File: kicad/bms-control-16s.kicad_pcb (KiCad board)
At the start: 2 copper layers, 120 x 65 mm, 131 parts, among them J1 TempBtn, J2 UEXT, J3 USB_B_Micro, J4 CAN, J5 Conn_02x09_Top_Bottom, J6 Conn_02x06_Odd_Even, J7 Conn_01x17, J8 Conn_01x02, P5 CONN_01X02, Q1 FCX495TA, U1 AP2210-3.3, U2 LMR16030, U3 STM32G0B1CETxN, U4 BQ76952, U5 ESP32-C3-MINI-1, U6 TJA1042T-3, Y1 8MHz

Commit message: v0.1 design ready for review
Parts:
- removed C34: 100n, LibreSolar:C_0603_1608
- removed D10: USBLC6-2SC6, LibreSolar:SOT-23-6
- removed J6: Conn_02x06_Odd_Even, Connector_PinSocket_2.54mm:PinSocket_2x06_P2.54mm_Vertical
- removed J7: Conn_01x17, Connector_PinHeader_2.54mm:PinHeader_1x17_P2.54mm_Vertical
- removed JP1: Jumper_NC_Small, Connector_PinHeader_2.54mm:PinHeader_1x02_P2.54mm_Vertical
- removed P5: CONN_01X02, Connector_PinHeader_2.54mm:PinHeader_1x02_P2.54mm_Vertical
- removed the REF** at (84.0, 101.0)
- removed SWD1: ST_Nucleo_SWD_5p, Connector_PinHeader_2.54mm:PinHeader_1x05_P2.54mm_Vertical
- added C44: 1µF, LibreSolar:C_0603_1608, F.Cu at (147.6, 61.4)
- added C45: 100pF, LibreSolar:C_0603_1608, F.Cu at (174.0, 67.5)
- added D9: D_Schottky, Diode_SMD:D_SOD-128, F.Cu at (133.0, 106.0)
- added FID1: Fiducial, Fiducial:Fiducial_1mm_Mask2mm, F.Cu at (101.0, 117.5)
- added FID2: Fiducial, Fiducial:Fiducial_1mm_Mask2mm, F.Cu at (179.9, 65.2)
- added J10: Conn_01x06, Connector_PinSocket_2.00mm:PinSocket_1x06_P2.00mm_Vertical, B.Cu at (156.0, 64.0)
- added J9: Conn_01x06, Connector_PinSocket_2.00mm:PinSocket_1x06_P2.00mm_Vertical, B.Cu at (156.0, 111.0)
- added TP10: CHG, TestPoint:TestPoint_Pad_D1.5mm, F.Cu at (159.0, 114.2)
- added TP11: CAN_H, TestPoint:TestPoint_Pad_D1.5mm, F.Cu at (120.5, 73.4)
- added TP12: SHUT, TestPoint:TestPoint_Pad_D1.5mm, F.Cu at (150.4, 58.8)
- added TP13: ALERT, TestPoint:TestPoint_Pad_D1.5mm, F.Cu at (150.4, 63.6)
- added TP14: SW_PWR, TestPoint:TestPoint_Pad_D1.5mm, F.Cu at (119.1, 104.9)
- added TP15: WAKE, TestPoint:TestPoint_Pad_D1.5mm, F.Cu at (130.8, 90.7)
- added TP2: CAN_L, TestPoint:TestPoint_Pad_D1.5mm, F.Cu at (117.9, 72.1)
- added TP3: REG1, TestPoint:TestPoint_Pad_D1.5mm, F.Cu at (156.5, 60.5)
- added TP4: PDSG, TestPoint:TestPoint_Pad_D1.5mm, F.Cu at (159.5, 60.5)
- added TP8: DSG, TestPoint:TestPoint_Pad_D1.5mm, F.Cu at (162.5, 60.5)
- added TP9: CD, TestPoint:TestPoint_Pad_D1.5mm, F.Cu at (162.2, 114.2)
- C27: value 100p -> 100pF
- C28: value 100n -> 100nF
- C30: value 470nF -> 680nF
- D1: value BAV70 -> 100V; footprint LibreSolar:SOT-23 -> Diode_SMD:D_SOD-123
- D6: value BAV70 -> D_Schottky; footprint LibreSolar:SOT-23 -> Diode_SMD:D_SOD-123F
- H1, H2, H3: footprint MountingHole:MountingHole_3.2mm_M3_Pad -> MountingHole:MountingHole_3.2mm_M3
- J1: value TempBtn -> MicroFit 2x7; footprint Connector_Molex:Molex_Micro-Fit_3.0_43045-0600_2x03_P3.00mm_Horizontal -> Connector_Molex:Molex_Micro-Fit_3.0_43045-1410_2x07-1MP_P3.00mm_Horizontal
- J4: value CAN -> Conn_01x06; footprint Connector_Molex:Molex_Micro-Fit_3.0_43045-0600_2x03_P3.00mm_Horizontal -> LibreSolar:Wuerth_WR-WST_2x03_P2.54_DBG
- J5: value Conn_02x09_Top_Bottom -> MicroFit 2x9; footprint Connector_Molex:Molex_Micro-Fit_3.0_43045-1800_2x09_P3.00mm_Horizontal -> Connector_Molex:Molex_Micro-Fit_3.0_43045-1810_2x09-1MP_P3.00mm_Horizontal
- R18, R21: footprint LibreSolar:R_0603_1608 -> LibreSolar:R_1206_3216
- R25: value 120 -> 1M; footprint LibreSolar:R_1206_3216 -> LibreSolar:R_0603_1608
- TP1: footprint TestPoint:TestPoint_Pad_D2.0mm -> TestPoint:TestPoint_Pad_D1.5mm
- TP5: value Regout -> REG1; footprint LibreSolar:TestPoint_1mm_pad -> TestPoint:TestPoint_Pad_D1.5mm
- TP6, TP7: footprint LibreSolar:TestPoint_1mm_pad -> TestPoint:TestPoint_Pad_D1.5mm
- moved H3 98.2 mm to (178.0, 116.0)
- moved LOGO1 92.1 mm to (170.6, 59.5)
- moved S1 64.0 mm to (104.5, 109.0), turned to 180 degrees
- moved R54 59.5 mm to (111.5, 104.0), turned to 180 degrees
- moved H2 58.7 mm to (178.0, 59.0)
- moved R53 57.3 mm to (111.5, 102.5), turned to 0 degrees
- moved LOGO2 54.7 mm to (143.2, 97.9)
- moved H1 53.3 mm to (119.0, 87.5)
- moved TP7 51.1 mm to (105.9, 75.3)
- moved TP6 50.5 mm to (108.6, 75.3)
- moved R25 48.9 mm to (139.5, 112.0), turned to 180 degrees
- moved J4 48.5 mm to (135.4, 66.2), turned to -90 degrees
- moved R26 43.7 mm to (144.1, 56.1), turned to 180 degrees
- moved C46 42.3 mm to (100.5, 62.5), turned to 90 degrees
- moved REF** 41.0 mm to (172.5, 108.0)
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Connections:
- net Net-(C39-Pad1) renamed /BQ76952/BREG_IN
- C37 pad 1: /BQ76952/REG1 -> /REG1
- D1 pad 1: /BAT+ -> /Power Supply/VIN
- D1 pad 2: unconnected-(D1-Pad2) -> /BAT+
- D2 pad 2: /CHG+ -> /CD
- D3 pad 2: Net-(D3-Pad2) -> /USB_D-
- D4 pad 2: Net-(D4-Pad2) -> /USB_D+
- D6 pad 1: /Power Supply/RGO -> +5V
- D6 pad 2: +5V -> /BQ76952/REG2
- D8 pad 3: unconnected-(D8-Pad3) -> GND
- J1 pad 1: /TEMP1 -> GND
- J1 pad 2: /TEMP2 -> GND
- J1 pad 4: GND -> unconnected-(J1-Pad4)
- J1 pad 6: /BTN_2 -> /CAN_L
- J3 pad 2: Net-(D3-Pad2) -> /USB_D-
- J3 pad 3: Net-(D4-Pad2) -> /USB_D+
- J4 pad 1: /CAN_H -> +3V3
- J4 pad 2: /CAN_L -> /SWDIO
- J4 pad 4: /CAN_H -> /SWCLK
- J4 pad 5: /CAN_L -> /DBG_RX
- J4 pad 6: GND -> /DBG_TX
- R20 pad 1: /PGND -> /PACK-
- R22 pad 2: /LED1 -> /LED_RED
- R23 pad 2: /LED2 -> /LED_GREEN
- R25 pad 1: Net-(JP1-Pad2) -> /Power Supply/VIN
- R25 pad 2: /CAN_L -> /REG1
- R32 pad 1: /USB_D- -> /ESP_USB_D-
- R32 pad 2: Net-(D3-Pad2) -> /USB_D-
- R33 pad 1: /USB_D+ -> /ESP_USB_D+
- R33 pad 2: Net-(D4-Pad2) -> /USB_D+
- R35 pad 2: /STM32 MCU/BOOT0 -> /SWCLK
- R55 pad 2: /STM32 MCU/I2C2_PULLUP -> +3V3
- R56 pad 2: /STM32 MCU/I2C2_PULLUP -> +3V3
- TP5 pad 1: /Power Supply/RGO -> /REG1
- U2 pad 3: /Power Supply/EN -> /REG1
- U3 pad 20: unconnected-(U3-Pad20) -> /BQ76952/RST_SHUT
- U3 pad 29: /STM32 MCU/USART1_TX -> /DBG_TX
- U3 pad 32: /STM32 MCU/USART1_RX -> /DBG_RX
- U3 pad 33: /STM32 MCU/USB_DM -> /USB_D-
- U3 pad 34: /STM32 MCU/USB_DP -> /USB_D+
- U3 pad 35: /STM32 MCU/SWDIO -> /SWDIO
- U3 pad 36: /STM32 MCU/SWCLK -> /SWCLK
- U4 pad 34: unconnected-(U4-Pad34) -> /BQ76952/REG2
- U4 pad 35: /BQ76952/REG1 -> /REG1
- U4 pad 40: /BQ76952/PCHG -> unconnected-(U4-Pad40)
- U5 pad 26: /USB_D- -> /ESP_USB_D-
- U5 pad 27: /USB_D+ -> /ESP_USB_D+
- U5 pad 30: /UEXT_RX -> /DBG_RX
- U5 pad 31: /UEXT_TX -> /DBG_TX
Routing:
- net +3V3: track 0.00 -> 189.4 mm, vias 0 -> 11
- net +5V: track 0.00 -> 144.3 mm, vias 0 -> 2
- net /ALERT: track 0.00 -> 108.2 mm, vias 0 -> 7
- net /SW_PWR: track 0.00 -> 101.4 mm, vias 0 -> 5
- net /LED_RED: track 0.00 -> 96.4 mm, vias 0 -> 4
- net /TEMP4: track 0.00 -> 90.8 mm
- net /LED_GREEN: track 0.00 -> 88.8 mm, vias 0 -> 4
- net /BTN_1: track 0.00 -> 82.4 mm, vias 0 -> 3
- net /REG1: track 0.00 -> 75.7 mm
- net GND: track 0.00 -> 72.7 mm, vias 1 -> 82
- net /CHG: track 0.00 -> 62.2 mm
- net /BQ_MISO_SDA: track 0.00 -> 59.4 mm, vias 0 -> 5
- net /BQ_SCK_SCL: track 0.00 -> 57.0 mm, vias 0 -> 5
- net /TEMP2: track 0.00 -> 56.5 mm, vias 0 -> 2
- net /DBG_RX: track 0.00 -> 56.1 mm, vias 0 -> 3
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- added copper zone on F.Cu, net +5V
- added copper zone on F.Cu, net /BQ76952/BREG_IN
- added copper zone on F.Cu, net /Power Supply/VIN
- added copper zone on F.Cu, net GND
- removed copper zone on F.Cu, net +3V3
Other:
- board size 120 x 65 mm -> 88 x 65 mm
- board text added: "2-layer PCB 35µm copper thickness Silkscreen top only"
- board text added: "v0.1"
- board text removed: "2-layer PCB 70µm copper thickness Silkscreen top only"

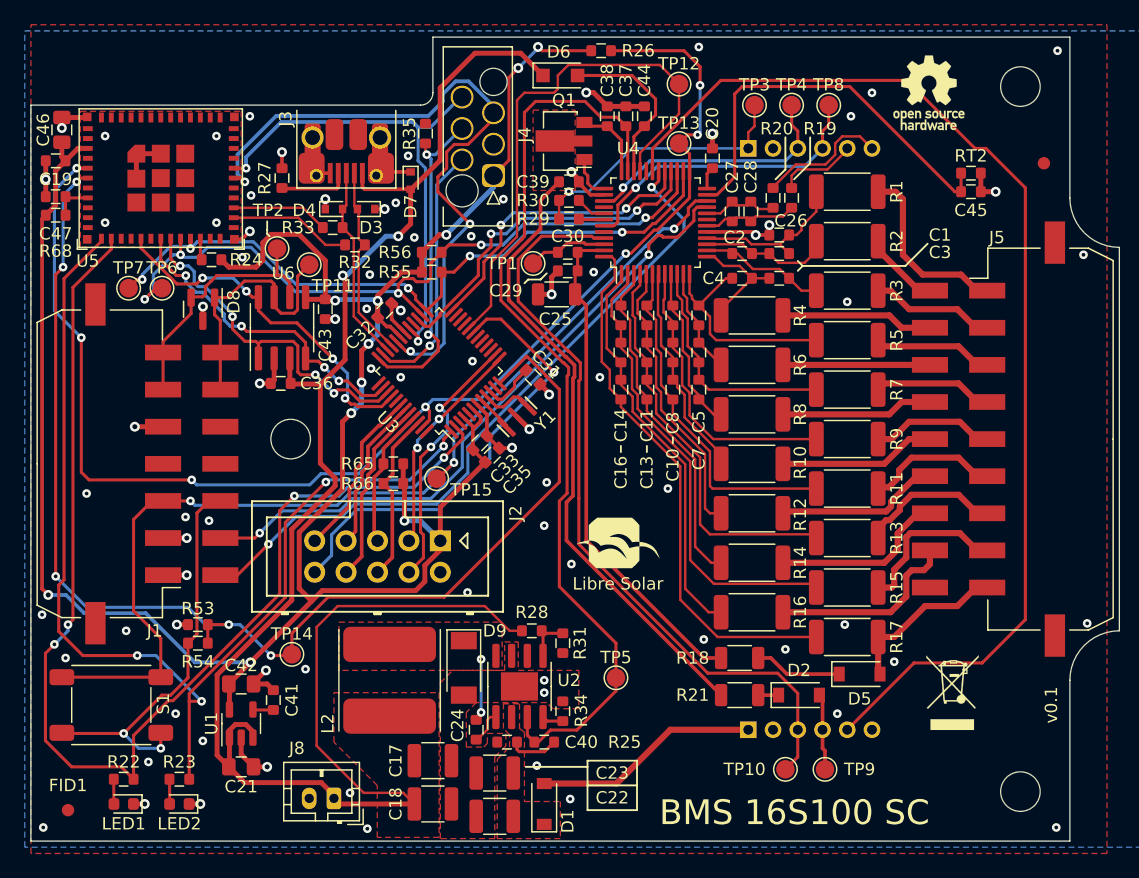
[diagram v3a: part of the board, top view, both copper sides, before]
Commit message: Updates based on review comments (v0.2)
This is the design revision that was ordered for the first prototype build.

The pinout of the cell connector and the board-to-board connector changed
compared to v0.1, hence it got a minor revision update.

The control board is now a 4-layer board to improve the grounding of the
PCB. Various other suggested improvements from the design review are also
included in this update.

Fixes #11, #12, #13, #17, #18, #19
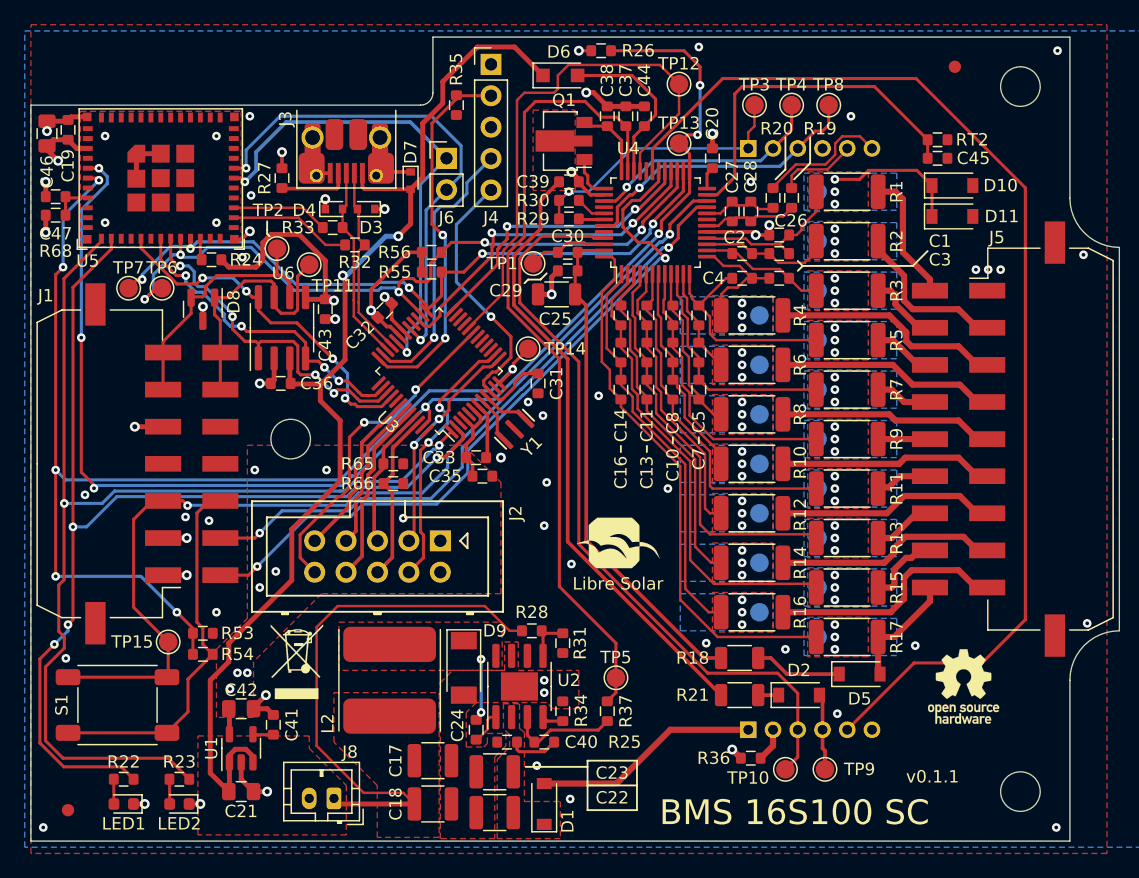
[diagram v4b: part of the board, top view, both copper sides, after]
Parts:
- added D10: 100V, Diode_SMD:D_SOD-123, F.Cu at (172.5, 67.0)
- added D11: 3.6V, Diode_SMD:D_SOD-123, F.Cu at (172.5, 69.5)
- added J6: Conn_01x02, Connector_PinHeader_2.54mm:PinHeader_1x02_P2.54mm_Vertical, F.Cu at (131.6, 64.8)
- added R36: 0R, LibreSolar:R_0603_1608, F.Cu at (156.2, 113.3)
- added R37: 0R, LibreSolar:R_0603_1608, F.Cu at (144.6, 109.5)
- added TP16: TestPoint, TestPoint:TestPoint_Pad_D1.5mm, B.Cu at (161.6, 67.5)
- added TP17: TestPoint, TestPoint:TestPoint_Pad_D1.5mm, B.Cu at (161.6, 71.5)
- added TP18: TestPoint, TestPoint:TestPoint_Pad_D1.5mm, B.Cu at (161.6, 75.5)
- added TP19: TestPoint, TestPoint:TestPoint_Pad_D1.5mm, B.Cu at (156.9, 77.5)
- added TP20: TestPoint, TestPoint:TestPoint_Pad_D1.5mm, B.Cu at (161.6, 79.5)
- added TP21: TestPoint, TestPoint:TestPoint_Pad_D1.5mm, B.Cu at (156.9, 81.5)
- added TP22: TestPoint, TestPoint:TestPoint_Pad_D1.5mm, B.Cu at (161.6, 83.5)
- added TP23: TestPoint, TestPoint:TestPoint_Pad_D1.5mm, B.Cu at (156.9, 85.5)
- added TP24: TestPoint, TestPoint:TestPoint_Pad_D1.5mm, B.Cu at (161.6, 87.5)
- added TP25: TestPoint, TestPoint:TestPoint_Pad_D1.5mm, B.Cu at (156.9, 89.5)
- added TP26: TestPoint, TestPoint:TestPoint_Pad_D1.5mm, B.Cu at (161.6, 91.5)
- added TP27: TestPoint, TestPoint:TestPoint_Pad_D1.5mm, B.Cu at (156.9, 93.5)
- added TP28: TestPoint, TestPoint:TestPoint_Pad_D1.5mm, B.Cu at (161.6, 95.5)
- added TP29: TestPoint, TestPoint:TestPoint_Pad_D1.5mm, B.Cu at (156.9, 97.5)
- added TP30: TestPoint, TestPoint:TestPoint_Pad_D1.5mm, B.Cu at (161.6, 99.5)
- added TP31: TestPoint, TestPoint:TestPoint_Pad_D1.5mm, B.Cu at (156.9, 101.5)
- added TP32: TestPoint, TestPoint:TestPoint_Pad_D1.5mm, B.Cu at (161.6, 103.5)
- C17, C18: value 47µ -> 47µF
- C21, C22, C23, C42: value 2.2µ -> 2.2µF
- C24, C31, C32, C33, C36, C40, C43: value 100n -> 100nF
- C35: value 4.7u -> 4.7µF
- C41: value 100p -> 100pF
- J4: value Conn_01x06 -> Conn_01x05; footprint LibreSolar:Wuerth_WR-WST_2x03_P2.54_DBG -> Connector_PinHeader_2.54mm:PinHeader_1x05_P2.54mm_Vertical
- moved REF** 53.1 mm to (119.5, 105.5)
- moved LOGO1 48.1 mm to (173.4, 107.5)
- moved TP14 31.2 mm to (138.2, 80.2), turned to -90 degrees
- moved TP15 25.4 mm to (109.1, 103.9)
- moved FID2 10.6 mm to (172.7, 57.4)
- moved J4 9.00 mm to (135.2, 57.2), turned to 0 degrees
- moved C45 3.82 mm to (171.3, 64.8)
- moved RT2 3.82 mm to (171.3, 63.3)
- moved R35 3.40 mm to (132.4, 60.5), turned to 90 degrees
- moved C19 2.69 mm to (101.0, 62.5), turned to 90 degrees
- moved C21 2.00 mm to (115.0, 116.0)
- moved C41 2.00 mm to (117.6, 110.6)
- moved C42 2.00 mm to (115.0, 109.3)
- moved U1 2.00 mm to (115.0, 112.5)
- moved C35 1.88 mm to (134.5, 90.5), turned to 0 degrees
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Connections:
- C31 pad 1: /STM32 MCU/~{RESET} -> /NRST
- J10 pad 2: unconnected-(J10-Pad2) -> /PDSG
- J10 pad 3: /PDSG -> /DSG
- J10 pad 4: /DSG -> unconnected-(J10-Pad4)
- J4 pad 2: /SWDIO -> /SWCLK
- J4 pad 4: /SWCLK -> /SWDIO
- J4 pad 5: /DBG_RX -> /NRST
- J5 pad 1: /C1- -> GND
- J5 pad 10: /C1+ -> /C1-
- J5 pad 11: /C3+ -> /C2+
- J5 pad 12: /C5+ -> /C4+
- J5 pad 13: /C7+ -> /C6+
- J5 pad 14: /C9+ -> /C8+
- J5 pad 15: /C11+ -> /C10+
- J5 pad 16: /C13+ -> /C12+
- J5 pad 17: /C15+ -> /C14+
- J5 pad 18: unconnected-(J5-Pad18) -> /C16+
- J5 pad 2: /C2+ -> /C1+
- J5 pad 3: /C4+ -> /C3+
- J5 pad 4: /C6+ -> /C5+
- J5 pad 5: /C8+ -> /C7+
- J5 pad 6: /C10+ -> /C9+
- J5 pad 7: /C12+ -> /C11+
- J5 pad 8: /C14+ -> /C13+
- J5 pad 9: /C16+ -> /C15+
- J9 pad 2: GND -> Net-(J9-Pad2)
- R25 pad 2: /REG1 -> /Power Supply/EN
- U2 pad 3: /REG1 -> /Power Supply/EN
- U3 pad 10: /STM32 MCU/~{RESET} -> /NRST
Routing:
- net +3V3: track 189.4 -> 46.3 mm, vias 11 -> 13
- net /NRST: track 0.00 -> 25.8 mm, vias 0 -> 1
- net /DBG_RX: track 56.1 -> 39.7 mm, vias 3 -> 2
- net /BQ76952/VC0: track 13.0 -> 24.1 mm, vias 0 -> 3
- net /REG1: track 75.7 -> 65.2 mm
- net /UEXT_SSEL: track 36.8 -> 26.9 mm, vias 1 -> 2
- net /Power Supply/EN: track 0.00 -> 8.86 mm
- net /LED_RED: track 96.4 -> 87.6 mm
- net /SW_PWR: track 101.4 -> 94.1 mm, vias 5 -> 6
- net /C1+: track 6.25 -> 13.3 mm
- net /C14+: track 12.9 -> 6.16 mm
- net /C12+: track 11.5 -> 5.01 mm
- net GND: track 72.7 -> 66.3 mm, vias 82 -> 64
- net /C3+: track 12.1 -> 18.4 mm
- net /C10+: track 10.8 -> 4.56 mm
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- added copper zone on B.Cu, net +3V3
- added copper zone on F.Cu, net +3V3
- added copper zone on B.Cu, net /BQ76952/VC0
- added copper zone on F.Cu, net /BQ76952/VC0
- added copper zone on B.Cu, net /BQ76952/VC1
- added copper zone on F.Cu, net /BQ76952/VC1
- added copper zone on B.Cu, net /BQ76952/VC10
- added copper zone on F.Cu, net /BQ76952/VC10
- added copper zone on B.Cu, net /BQ76952/VC11
- added copper zone on F.Cu, net /BQ76952/VC11
- added copper zone on B.Cu, net /BQ76952/VC12
- added copper zone on F.Cu, net /BQ76952/VC12
- added copper zone on B.Cu, net /BQ76952/VC13
- added copper zone on F.Cu, net /BQ76952/VC13
- added copper zone on B.Cu, net /BQ76952/VC14
- added copper zone on F.Cu, net /BQ76952/VC14
- added copper zone on B.Cu, net /BQ76952/VC15
- added copper zone on F.Cu, net /BQ76952/VC15
- added copper zone on B.Cu, net /BQ76952/VC16
- added copper zone on F.Cu, net /BQ76952/VC16
- added copper zone on B.Cu, net /BQ76952/VC2
- added copper zone on F.Cu, net /BQ76952/VC2
- added copper zone on B.Cu, net /BQ76952/VC3
- added copper zone on F.Cu, net /BQ76952/VC3
- added copper zone on B.Cu, net /BQ76952/VC4
- added copper zone on F.Cu, net /BQ76952/VC4
- added copper zone on B.Cu, net /BQ76952/VC5
- added copper zone on F.Cu, net /BQ76952/VC5
- added copper zone on B.Cu, net /BQ76952/VC6
- added copper zone on F.Cu, net /BQ76952/VC6
- added copper zone on B.Cu, net /BQ76952/VC7
- added copper zone on F.Cu, net /BQ76952/VC7
- added copper zone on B.Cu, net /BQ76952/VC8
- added copper zone on F.Cu, net /BQ76952/VC8
- added copper zone on B.Cu, net /BQ76952/VC9
- added copper zone on F.Cu, net /BQ76952/VC9
- added copper zone on In1.Cu, net GND
- added copper zone on In2.Cu, net GND
- removed copper zone on B.Cu, net GND
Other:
- copper layers 2 -> 4
- board text added: "4-layer PCB 35µm copper thickness Silkscreen top only"
- board text added: "v0.1.1"
- board text removed: "2-layer PCB 35µm copper thickness Silkscreen top only"
- board text removed: "v0.1"
